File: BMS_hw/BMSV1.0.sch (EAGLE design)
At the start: 161 parts, among them IC1 MC33771BEP, IC2 SFH6156, J2 NTC, X2 87758-1816

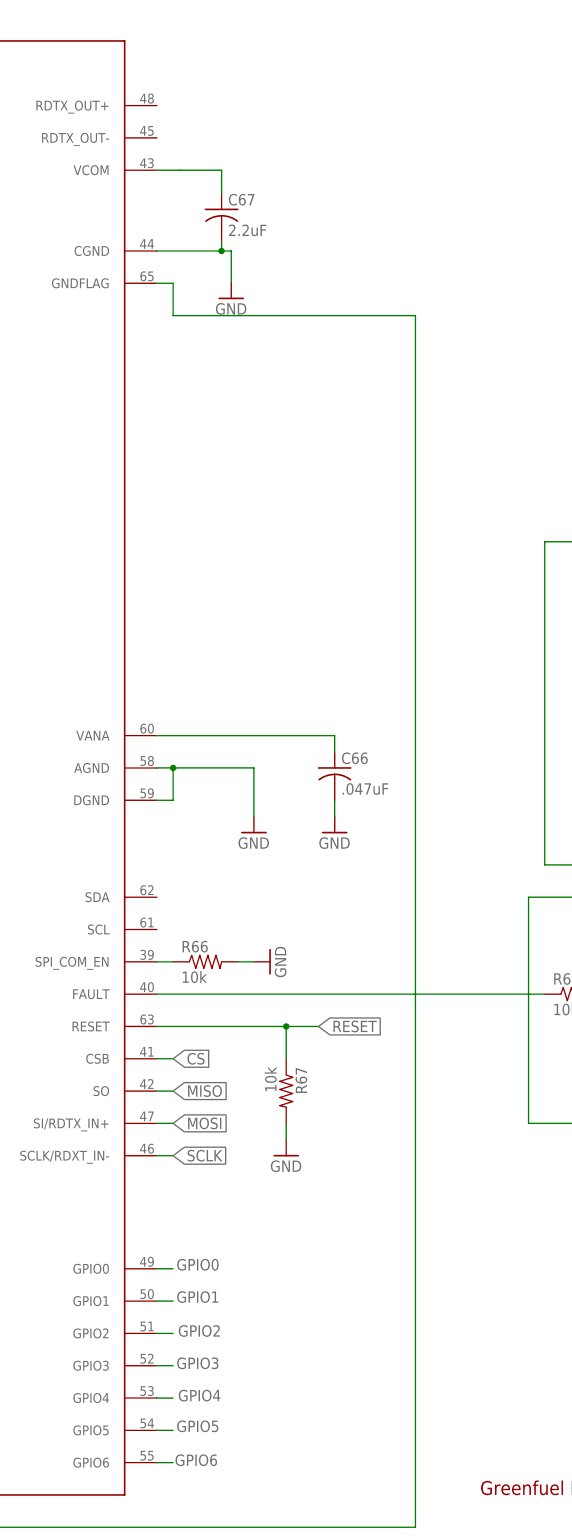
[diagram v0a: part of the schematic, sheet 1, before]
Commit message: updated after NXP review
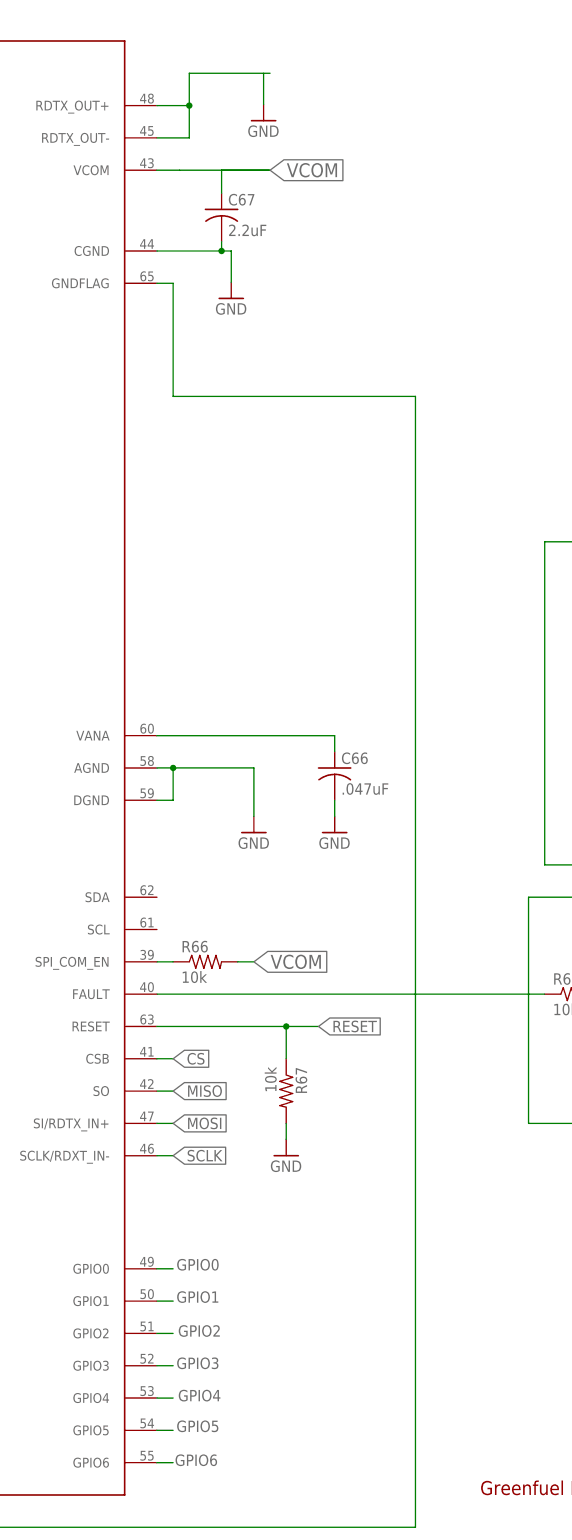
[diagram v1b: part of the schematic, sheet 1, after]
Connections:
- removed net N$28: C67.1, IC1.VCOM
- new net N$14: IC1.RDTX_OUT+, IC1.RDTX_OUT-
- net GND: no longer R66.2
- net VCOM: now also C67.1, IC1.VCOM, R66.2
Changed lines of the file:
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@@
 <part name="R64" library="adafruit" library_urn="urn:adsk.eagle:library:420" deviceset="R-US_" device="R0805" value="10k"/>
 <part name="R66" library="adafruit" library_urn="urn:adsk.eagle:library:420" deviceset="R-US_" device="R0805" value="10k"/>
-<part name="GND63" library="supply1" library_urn="urn:adsk.eagle:library:371" deviceset="GND" device=""/>
 <part name="R67" library="adafruit" library_urn="urn:adsk.eagle:library:420" deviceset="R-US_" device="R0805" value="10k"/>
 <part name="GND64" library="supply1" library_urn="urn:adsk.eagle:library:371" deviceset="GND" device=""/>
@@
 <part name="P-2" library="supply2" library_urn="urn:adsk.eagle:library:372" deviceset="V-" device=""/>
 <part name="P-3" library="supply2" library_urn="urn:adsk.eagle:library:372" deviceset="V-" device=""/>
+<part name="GND23" library="supply1" library_urn="urn:adsk.eagle:library:371" deviceset="GND" device=""/>
 </parts>
 <sheets>
@@
 <instance part="R64" gate="G$1" x="307.34" y="93.98"/>
 <instance part="R66" gate="G$1" x="248.92" y="99.06"/>
-<instance part="GND63" gate="1" x="259.08" y="99.06" rot="R90"/>
 <instance part="R67" gate="G$1" x="261.62" y="78.74" rot="R270"/>
 <instance part="GND64" gate="1" x="261.62" y="68.58"/>
@@
 <instance part="X2" gate="-18" x="342.9" y="116.84" rot="MR0"/>
 <instance part="FRAME1" gate="G$1" x="0" y="0"/>
+<instance part="GND23" gate="1" x="258.064" y="231.306"/>
 </instances>
 <busses>
@@
 <junction x="162.56" y="33.02"/>
 <pinref part="IC1" gate="G$1" pin="GNDFLAG"/>
-<wire x1="243.84" y1="200.66" x2="243.84" y2="205.74" width="0.1524" layer="91"/>
+<wire x1="243.84" y1="187.96" x2="243.84" y2="205.74" width="0.1524" layer="91"/>
 <wire x1="243.84" y1="205.74" x2="241.3" y2="205.74" width="0.1524" layer="91"/>
-<wire x1="281.94" y1="10.16" x2="281.94" y2="200.66" width="0.1524" layer="91"/>
-<wire x1="281.94" y1="200.66" x2="243.84" y2="200.66" width="0.1524" layer="91"/>
+<wire x1="281.94" y1="10.16" x2="281.94" y2="187.96" width="0.1524" layer="91"/>
+<wire x1="281.94" y1="187.96" x2="243.84" y2="187.96" width="0.1524" layer="91"/>
 </segment>
 <segment>
@@
 </segment>
 <segment>
-<pinref part="GND63" gate="1" pin="GND"/>
-<pinref part="R66" gate="G$1" pin="2"/>
-<wire x1="256.54" y1="99.06" x2="254" y2="99.06" width="0.1524" layer="91"/>
-</segment>
-<segment>
 <pinref part="GND64" gate="1" pin="GND"/>
 <pinref part="R67" gate="G$1" pin="2"/>
@@
 <wire x1="314.96" y1="132.08" x2="312.42" y2="132.08" width="0.1524" layer="91"/>
 <label x="307.34" y="132.08" size="1.778" layer="95"/>
+</segment>
+<segment>
+<pinref part="GND23" gate="1" pin="GND"/>
+<wire x1="258.064" y1="238.76" x2="258.064" y2="233.846" width="0.1524" layer="91"/>
 </segment>
 </net>
@@
 </segment>
 </net>
-<net name="N$28" class="0">
+<net name="VCOM" class="0">
 <segment>
 <pinref part="C67" gate="G$1" pin="1"/>
 <wire x1="251.46" y1="219.9" x2="251.46" y2="223.52" width="0.1524" layer="91"/>
-<wire x1="251.46" y1="223.52" x2="244.856" y2="223.52" width="0.1524" layer="91"/>
+<wire x1="251.46" y1="223.52" x2="259.08" y2="223.52" width="0.1524" layer="91"/>
+<wire x1="259.08" y1="223.52" x2="244.856" y2="223.52" width="0.1524" layer="91"/>
 <pinref part="IC1" gate="G$1" pin="VCOM"/>
 <wire x1="241.3" y1="223.52" x2="244.856" y2="223.52" width="0.1524" layer="91"/>
+<label x="259.08" y="223.52" size="2.1844" layer="95" xref="yes"/>
+</segment>
+<segment>
+<pinref part="R66" gate="G$1" pin="2"/>
+<wire x1="256.54" y1="99.06" x2="254" y2="99.06" width="0.1524" layer="91"/>
+<label x="256.54" y="99.06" size="2.1844" layer="95" xref="yes"/>
 </segment>
 </net>
@@
 </segment>
 </net>
+<net name="N$14" class="0">
+<segment>
+<pinref part="IC1" gate="G$1" pin="RDTX_OUT-"/>
+<wire x1="241.3" y1="228.6" x2="246.38" y2="228.6" width="0.1524" layer="91"/>
+<wire x1="246.38" y1="228.6" x2="246.38" y2="233.68" width="0.1524" layer="91"/>
+<pinref part="IC1" gate="G$1" pin="RDTX_OUT+"/>
+<wire x1="246.38" y1="233.68" x2="241.3" y2="233.68" width="0.1524" layer="91"/>
+<wire x1="246.38" y1="233.68" x2="246.38" y2="238.76" width="0.1524" layer="91"/>
+<junction x="246.38" y="233.68"/>
+<wire x1="246.38" y1="238.76" x2="259.08" y2="238.76" width="0.1524" layer="91"/>
+</segment>
+</net>

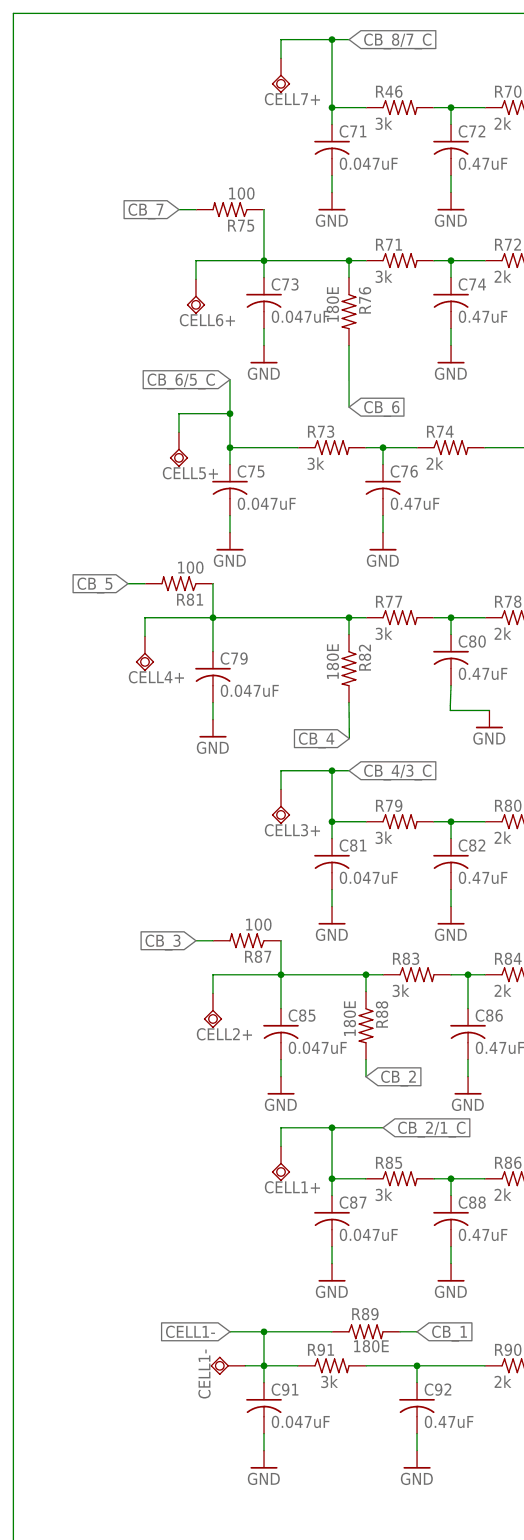
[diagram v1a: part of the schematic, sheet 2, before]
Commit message: Cell terminal pad replaced with specified size
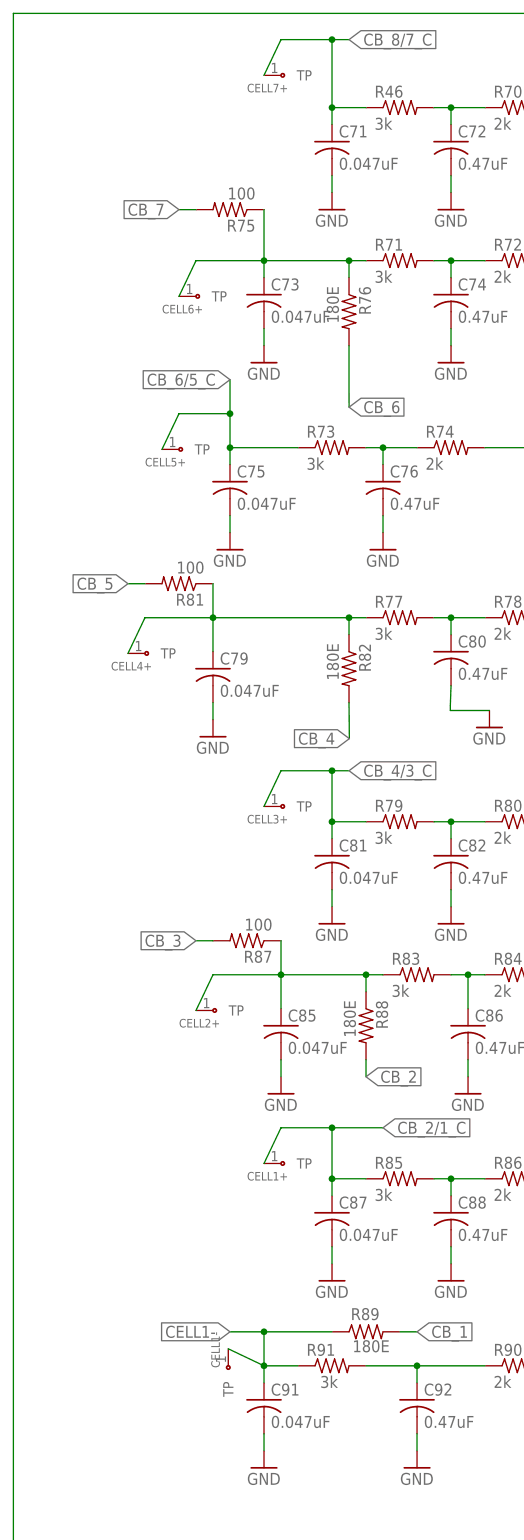
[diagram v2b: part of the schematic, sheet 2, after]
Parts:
- CELL1+, CELL1-, CELL10+, CELL11+, CELL12+, CELL13+, CELL14+, CELL2+, CELL3+, CELL4+, CELL5+, CELL6+, CELL7+, CELL8+, CELL9+: value TPSQTP20SQ -> GF_BMS_CELL_PADP_PAD; device testpad:TPSQTP20SQ -> GreenFuel:GF_BMS_CELL_PADP_PAD

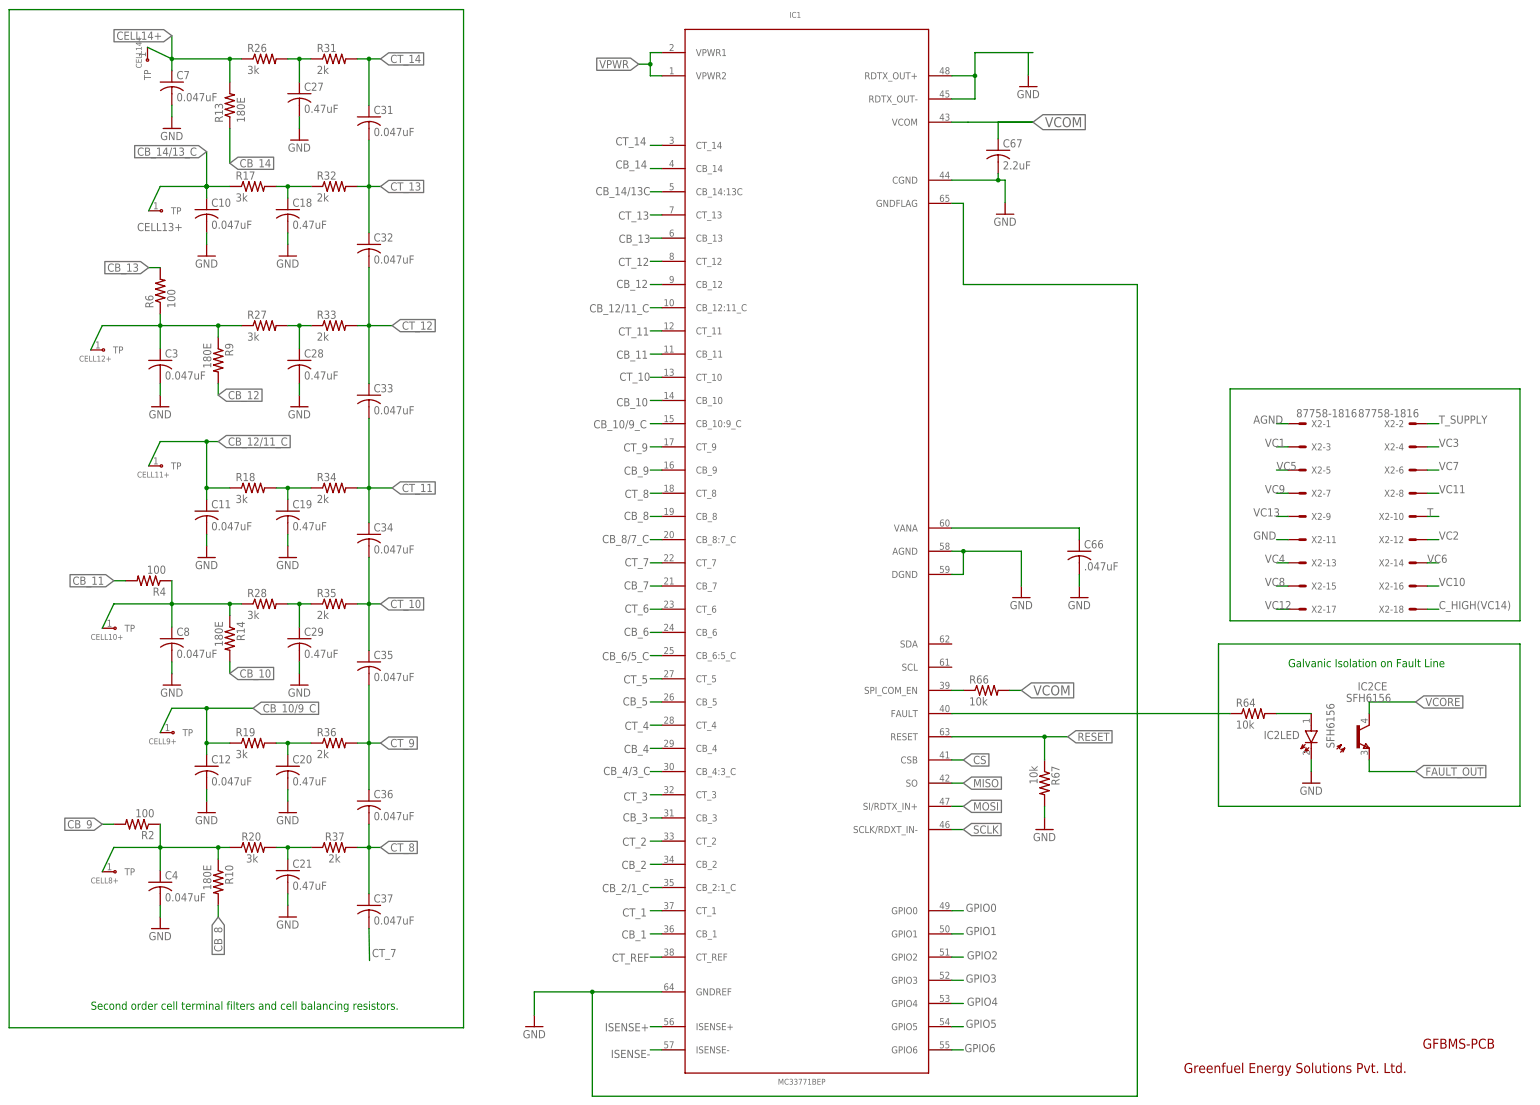
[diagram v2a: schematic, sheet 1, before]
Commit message: board schematic names and values changed
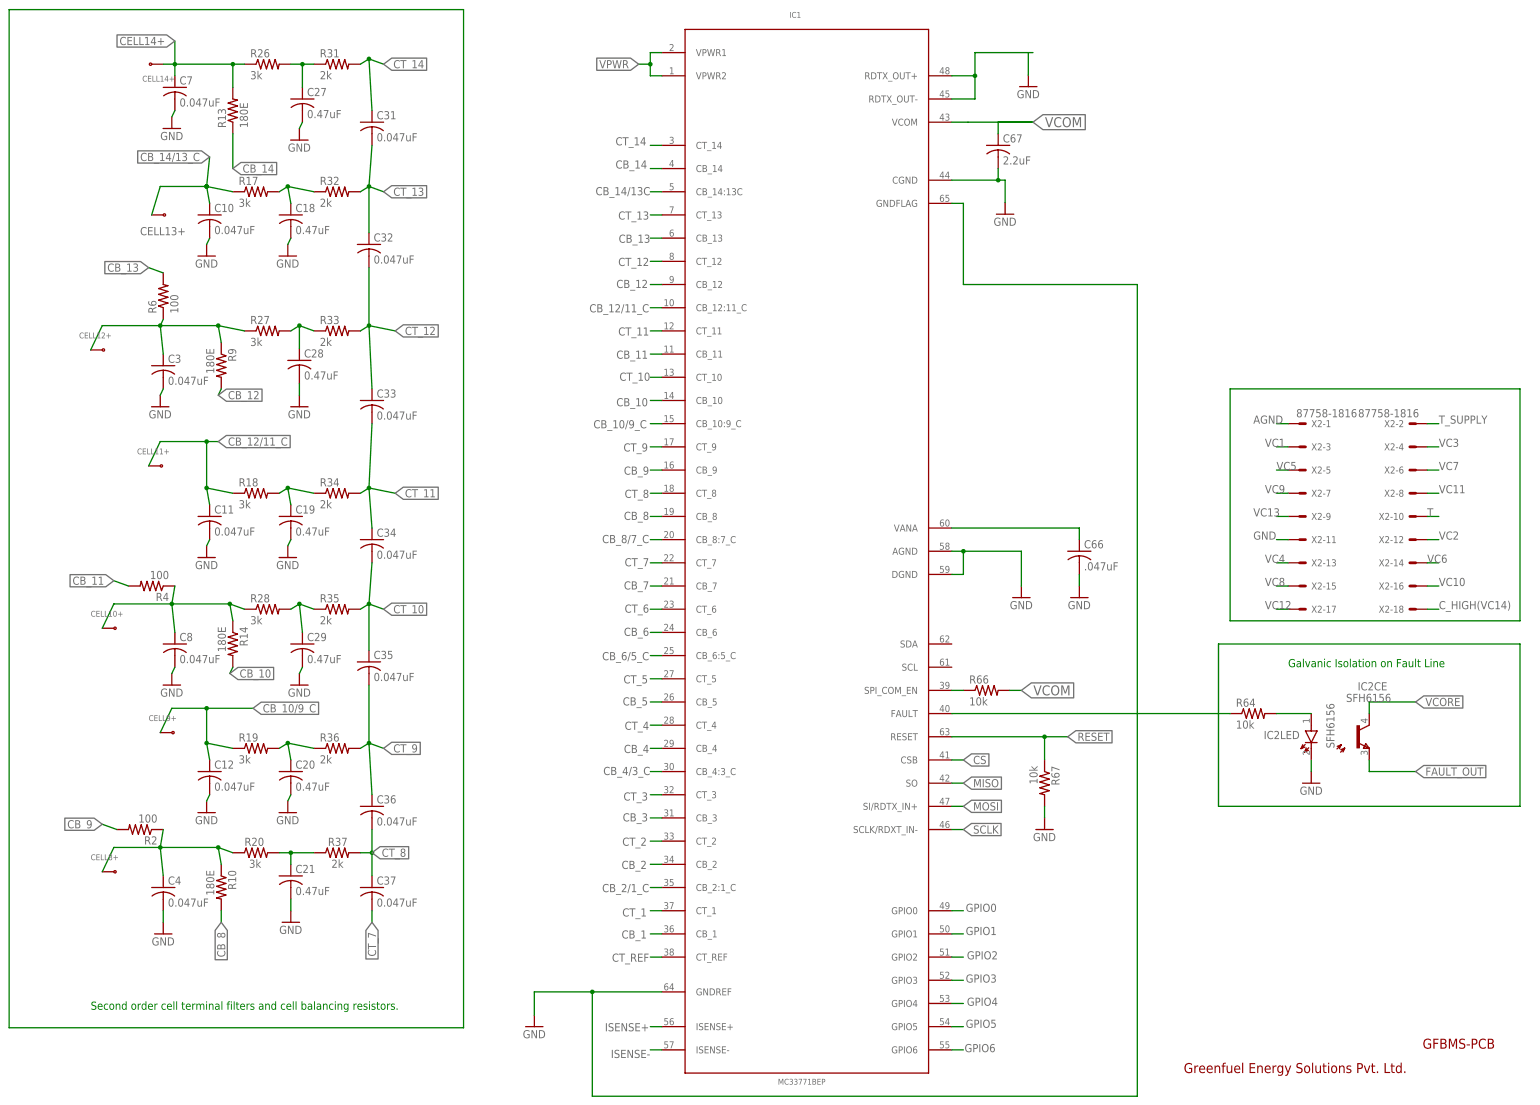
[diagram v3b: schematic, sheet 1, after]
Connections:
- net CB_10/9_C: now also CELL9+.S; no longer CELL9+.TP
- net CB_12/11_C: now also CELL11+.S; no longer CELL11+.TP
- net CB_13/12_C: now also CELL12+.S; no longer CELL12+.TP
- net CB_13/12_C1: now also CELL10+.S; no longer CELL10+.TP
- net CB_13/12_C2: now also CELL8+.S; no longer CELL8+.TP
- net CB_13/12_C6: now also CELL6+.S; no longer CELL6+.TP
- net CB_13/12_C7: now also CELL4+.S; no longer CELL4+.TP
- net CB_13/12_C8: now also CELL2+.S; no longer CELL2+.TP
- net CB_14/13_C: now also CELL13+.S; no longer CELL13+.TP
- net CB_2/1_C: now also CELL1+.S; no longer CELL1+.TP
- net CB_4/3_C: now also CELL3+.S; no longer CELL3+.TP
- net CB_6/5_C: now also CELL5+.S; no longer CELL5+.TP
- net CB_8/7_C: now also CELL7+.S; no longer CELL7+.TP
- net CELL1-: now also CELL1-.S; no longer CELL1-.TP
- net CELL14+: now also CELL14+.S; no longer CELL14+.TP
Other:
- moved on the sheet: C10, C11, C12, C18, C19, C20, C21, C27, C29, C3, C31, C33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

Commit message: Schematic componenet out of track are being retracked
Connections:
- removed net N$14: IC1.RDTX_OUT+, IC1.RDTX_OUT-
- net GND: now also IC1.RDTX_OUT+, IC1.RDTX_OUT-
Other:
- moved on the sheet: C28, C32, C35, CELL10+, CELL11+, CELL12+, CELL13+, CELL8+, CELL9+
